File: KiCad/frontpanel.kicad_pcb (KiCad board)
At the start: 2 copper layers, 26 parts, among them P1 CONN_02X13, P2 CONN_02X13

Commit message: some changes and improvments
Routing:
- net (no net): track 0.00 -> 1.27 mm
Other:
- board outline added: 139.7 x 88.9 mm
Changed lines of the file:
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@@
   (general
     (links 87)
-    (no_connects 1)
-    (area 97.689999 26.36 256.92 125.830001)
+    (no_connects 0)
+    (area 97.739999 26.36 256.92 125.780001)
     (thickness 1.6)
-    (drawings 6)
-    (tracks 413)
+    (drawings 18)
+    (tracks 414)
     (zones 0)
     (modules 26)
@@
     (pad_to_mask_clearance 0)
     (aux_axis_origin 0 0)
-    (visible_elements FFFFE77F)
+    (visible_elements FFFFF77F)
     (pcbplotparams
       (layerselection 0x00030_80000001)
@@
       (net 22 "Net-(AFF1-Pad22)"))
   )
-  (gr_line (start 97.79 125.73) (end 97.79 36.83) (angle 90) (layer Eco2.User) (width 0.2))
-  (gr_line (start 237.49 125.73) (end 97.79 125.73) (angle 90) (layer Eco2.User) (width 0.2))
-  (gr_line (start 237.49 36.83) (end 237.49 125.73) (angle 90) (layer Eco2.User) (width 0.2))
-  (gr_line (start 237.49 36.83) (end 97.79 36.83) (angle 90) (layer Eco2.User) (width 0.2))
+  (gr_line (start 99.06 36.83) (end 236.22 36.83) (layer Edge.Cuts) (width 0.1))
+  (gr_line (start 97.79 38.1) (end 97.79 124.46) (layer Edge.Cuts) (width 0.1))
+  (gr_line (start 236.22 125.73) (end 99.06 125.73) (layer Edge.Cuts) (width 0.1))
+  (gr_arc (start 99.06 124.46) (end 99.06 125.73) (angle 90) (layer Edge.Cuts) (width 0.1))
+  (gr_arc (start 236.22 124.46) (end 237.49 124.46) (angle 90) (layer Edge.Cuts) (width 0.1))
+  (gr_line (start 237.49 38.1) (end 237.49 124.46) (layer Edge.Cuts) (width 0.1))
+  (gr_arc (start 236.22 38.1) (end 236.22 36.83) (angle 90) (layer Edge.Cuts) (width 0.1))
+  (gr_arc (start 99.06 38.1) (end 97.79 38.1) (angle 90) (layer Edge.Cuts) (width 0.1))
+  (gr_circle (center 102.87 41.91) (end 101.346 42.164) (layer Edge.Cuts) (width 0.1))
+  (gr_circle (center 102.87 120.65) (end 101.346 120.65) (layer Edge.Cuts) (width 0.1))
+  (gr_circle (center 232.41 120.65) (end 230.886 120.65) (layer Edge.Cuts) (width 0.1))
+  (gr_circle (center 232.41 41.91) (end 230.886 41.91) (layer Edge.Cuts) (width 0.1))
+  (target plus (at 102.87 120.65) (size 5) (width 0.1) (layer Edge.Cuts))
+  (target plus (at 232.41 120.65) (size 5) (width 0.1) (layer Edge.Cuts))
+  (target plus (at 102.87 41.91) (size 5) (width 0.1) (layer Edge.Cuts))
+  (target plus (at 232.41 41.91) (size 5) (width 0.1) (layer Edge.Cuts))
   (dimension 88.9 (width 0.3) (layer Cmts.User)
     (gr_text "88,900 mm" (at 250.27 81.28 270) (layer Cmts.User)
@@
     (arrow2b (pts (xy 237.49 29.21) (xy 236.363496 29.796421)))
   )
+  (segment (start 236.22 124.46) (end 237.49 124.46) (width 0.25) (layer Dwgs.User) (net 0))
   (segment (start 182.88 81.28) (end 194.228601 69.931399) (width 0.25) (layer B.Cu) (net 5))
   (segment (start 194.228601 69.931399) (end 224.708601 69.931399) (width 0.25) (layer B.Cu) (net 5))

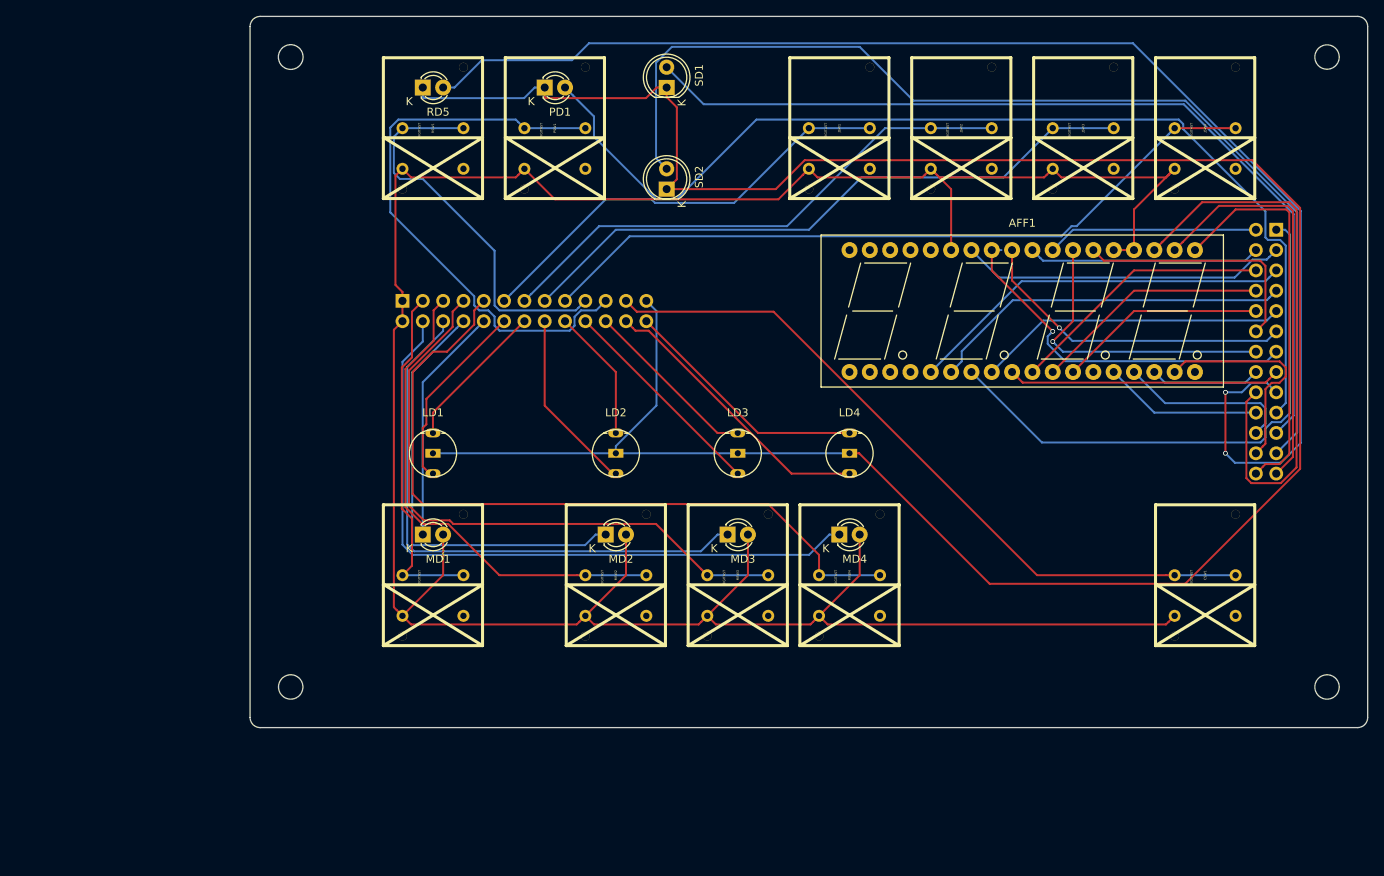
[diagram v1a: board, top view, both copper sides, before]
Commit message: Flipped the pinpads on the frontpanel board ...
... so that we don't have to twist the cables.
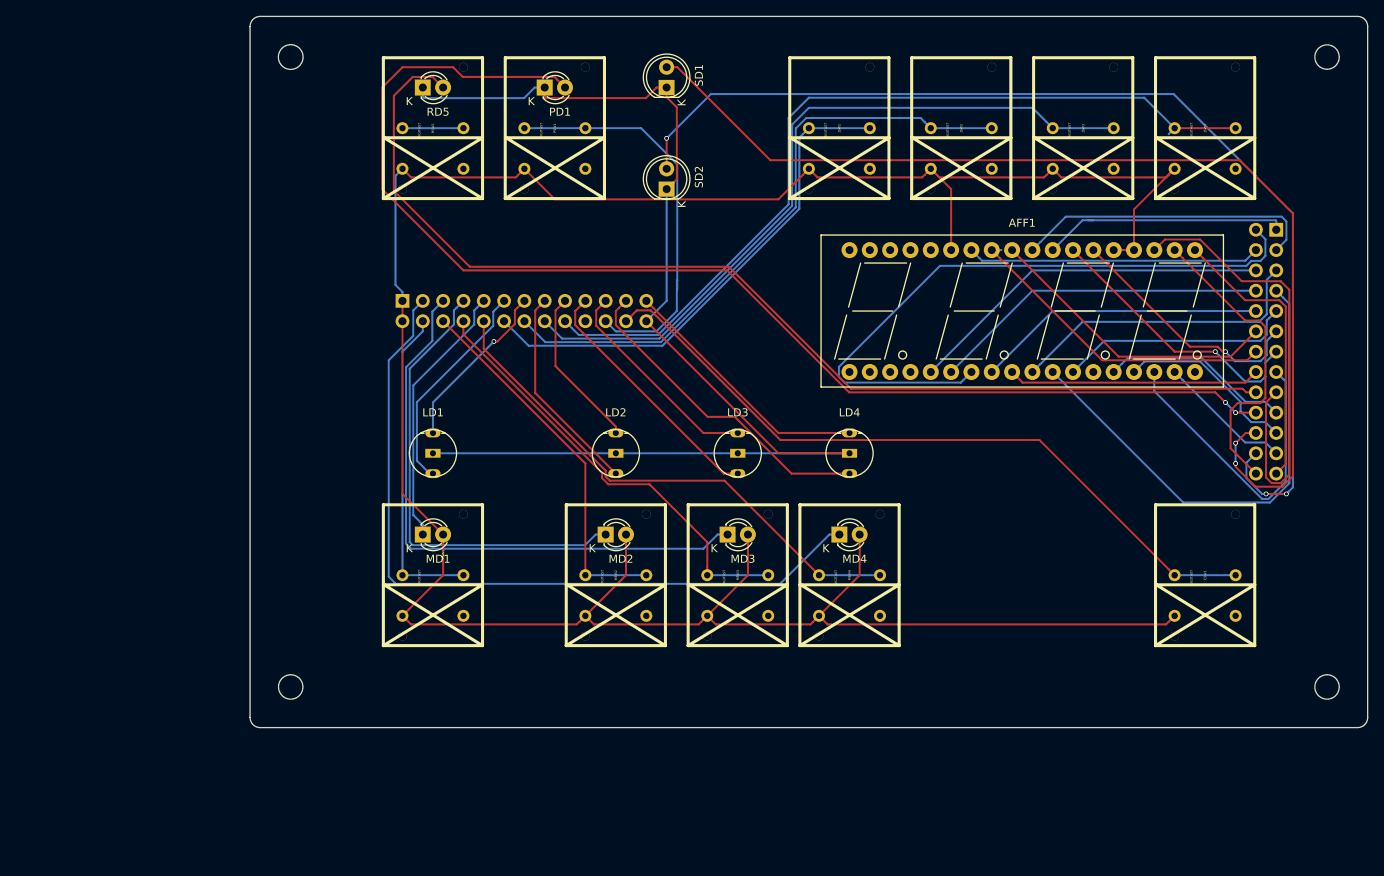
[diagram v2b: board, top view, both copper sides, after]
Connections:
- P1 pad 10: Net-(MD1-Pad1) -> Net-(MSW4-Pad0)
- P1 pad 11: Net-(JSW1-Pad0) -> Net-(LD1-Pad3)
- P1 pad 12: Net-(LD1-Pad3) -> Net-(JSW1-Pad0)
- P1 pad 13: Net-(JSW2-Pad0) -> Net-(LD1-Pad1)
- P1 pad 14: Net-(LD1-Pad1) -> Net-(JSW2-Pad0)
- P1 pad 15: Net-(JSW3-Pad0) -> Net-(LD2-Pad3)
- P1 pad 16: Net-(LD2-Pad3) -> Net-(JSW3-Pad0)
- P1 pad 17: Net-(JSW4-Pad0) -> Net-(LD2-Pad1)
- P1 pad 18: Net-(LD2-Pad1) -> Net-(JSW4-Pad0)
- P1 pad 19: Net-(P1-Pad19) -> Net-(LD3-Pad3)
- P1 pad 20: Net-(LD3-Pad3) -> Net-(P1-Pad20)
- P1 pad 21: Net-(P1-Pad21) -> Net-(LD3-Pad1)
- P1 pad 22: Net-(LD3-Pad1) -> Net-(P1-Pad22)
- P1 pad 23: Net-(CSW1-Pad0) -> Net-(LD4-Pad3)
- P1 pad 24: Net-(LD4-Pad3) -> Net-(CSW1-Pad0)
- P1 pad 25: Net-(LD1-Pad2) -> Net-(LD4-Pad1)
- P1 pad 26: Net-(LD4-Pad1) -> Net-(LD1-Pad2)
- P1 pad 3: Net-(MSW1-Pad0) -> Net-(MD4-Pad1)
- P1 pad 4: Net-(MD4-Pad1) -> Net-(MSW1-Pad0)
- P1 pad 5: Net-(MSW2-Pad0) -> Net-(MD3-Pad1)
- P1 pad 6: Net-(MD3-Pad1) -> Net-(MSW2-Pad0)
- P1 pad 7: Net-(MSW3-Pad0) -> Net-(MD2-Pad1)
- P1 pad 8: Net-(MD2-Pad1) -> Net-(MSW3-Pad0)
- P1 pad 9: Net-(MSW4-Pad0) -> Net-(MD1-Pad1)
- P2 pad 1: Net-(AFF1-Pad7) -> Net-(AFF1-Pad26)
- P2 pad 10: Net-(AFF1-Pad12) -> Net-(AFF1-Pad8)
- P2 pad 11: Net-(AFF1-Pad28) -> Net-(AFF1-Pad24)
- P2 pad 12: Net-(AFF1-Pad24) -> Net-(AFF1-Pad28)
- P2 pad 13: Net-(AFF1-Pad29) -> Net-(AFF1-Pad25)
- P2 pad 14: Net-(AFF1-Pad25) -> Net-(AFF1-Pad29)
- P2 pad 15: Net-(AFF1-Pad9) -> Net-(AFF1-Pad16)
- P2 pad 16: Net-(AFF1-Pad16) -> Net-(AFF1-Pad9)
- P2 pad 17: Net-(P2-Pad17) -> Net-(AFF1-Pad21)
- P2 pad 18: Net-(AFF1-Pad21) -> Net-(P2-Pad18)
- P2 pad 19: Net-(P2-Pad19) -> Net-(AFF1-Pad14)
- P2 pad 2: Net-(AFF1-Pad26) -> Net-(AFF1-Pad7)
- P2 pad 20: Net-(AFF1-Pad14) -> Net-(P2-Pad20)
- P2 pad 21: Net-(P2-Pad21) -> Net-(AFF1-Pad15)
- P2 pad 22: Net-(AFF1-Pad15) -> Net-(P2-Pad22)
- P2 pad 23: Net-(P2-Pad23) -> Net-(AFF1-Pad17)
- P2 pad 24: Net-(AFF1-Pad17) -> Net-(P2-Pad24)
- P2 pad 25: Net-(AFF1-Pad20) -> Net-(AFF1-Pad19)
- P2 pad 26: Net-(AFF1-Pad19) -> Net-(AFF1-Pad20)
- P2 pad 3: Net-(AFF1-Pad30) -> Net-(AFF1-Pad27)
- P2 pad 4: Net-(AFF1-Pad27) -> Net-(AFF1-Pad30)
- P2 pad 5: Net-(AFF1-Pad5) -> Net-(AFF1-Pad10)
- P2 pad 6: Net-(AFF1-Pad10) -> Net-(AFF1-Pad5)
- P2 pad 7: Net-(AFF1-Pad6) -> Net-(AFF1-Pad11)
- P2 pad 8: Net-(AFF1-Pad11) -> Net-(AFF1-Pad6)
- P2 pad 9: Net-(AFF1-Pad8) -> Net-(AFF1-Pad12)
- PD1 pad 2: Net-(P2-Pad19) -> Net-(P2-Pad20)
- PSW1 pad 0: Net-(P1-Pad21) -> Net-(P1-Pad22)
- RD5 pad 2: Net-(P2-Pad17) -> Net-(P2-Pad18)
- RSW1 pad 0: Net-(P1-Pad19) -> Net-(RSW1-Pad0)
- SD1 pad 2: Net-(P2-Pad21) -> Net-(P2-Pad22)
- SD2 pad 2: Net-(P2-Pad23) -> Net-(P2-Pad24)
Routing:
- net Net-(P2-Pad17): track 173.1 -> 0.00 mm, vias 2 -> 0
- net Net-(P2-Pad20): track 0.00 -> 158.5 mm, vias 0 -> 2
- net Net-(LD1-Pad2): track 307.9 -> 151.2 mm
- net Net-(P2-Pad18): track 0.00 -> 137.8 mm
- net Net-(P2-Pad24): track 0.00 -> 135.4 mm, vias 0 -> 3
- net Net-(P2-Pad23): track 134.5 -> 0.00 mm
- net Net-(P2-Pad22): track 0.00 -> 133.5 mm, vias 0 -> 2
- net Net-(P2-Pad19): track 131.7 -> 0.00 mm
- net Net-(P2-Pad21): track 114.2 -> 0.00 mm
- net Net-(P1-Pad21): track 72.4 -> 0.00 mm
- net Net-(P1-Pad22): track 0.00 -> 51.0 mm
- net Net-(P1-Pad19): track 49.2 -> 0.00 mm
- net Net-(AFF1-Pad11): track 29.6 -> 62.1 mm
- net Net-(MSW4-Pad0): track 93.0 -> 65.1 mm
- net Net-(AFF1-Pad16): track 13.8 -> 39.5 mm
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
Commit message: Reinforced power wires on frontpanel board
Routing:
- net Net-(AFF1-Pad22): track 327.0 -> 334.1 mm
- net Net-(LD1-Pad2): track 151.2 -> 150.4 mm
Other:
- net class Power added: clearance 0.2, trace_width 0.58, via_dia 0.6, via_drill 0.4

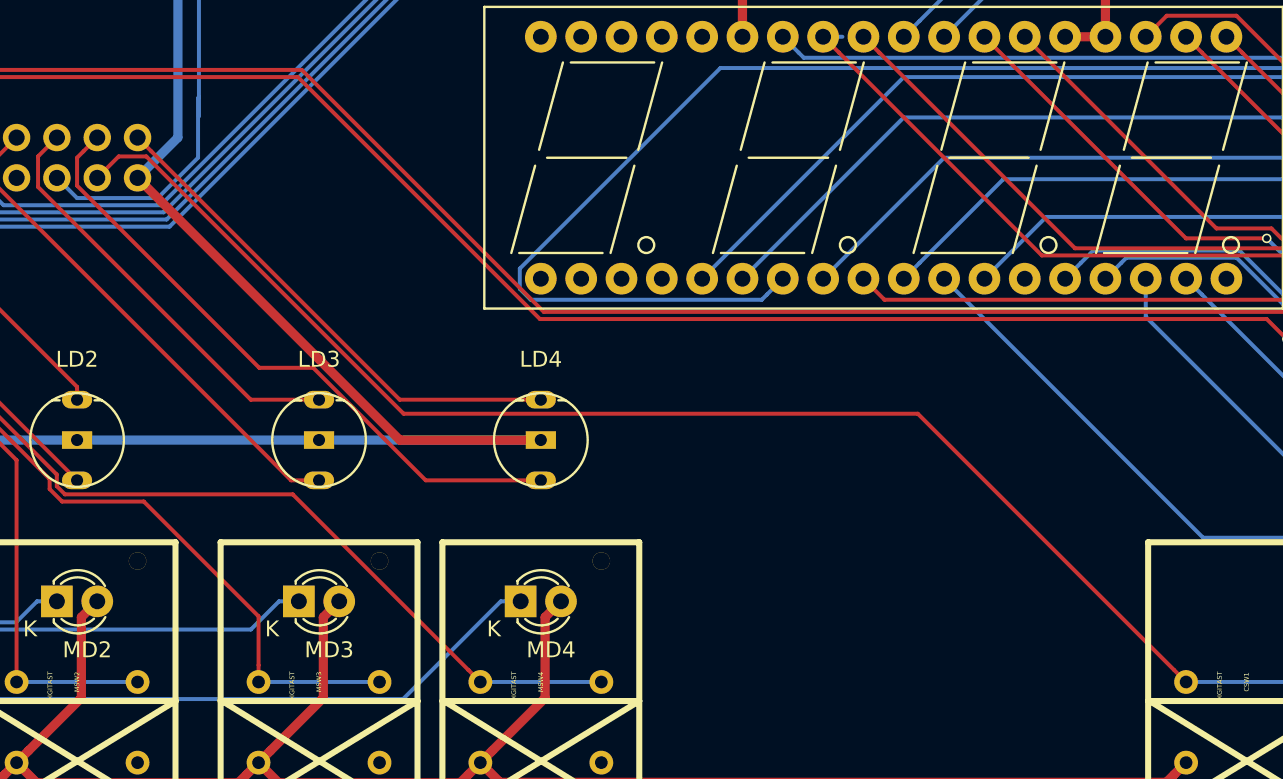
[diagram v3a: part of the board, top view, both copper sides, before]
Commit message: stripped some wires
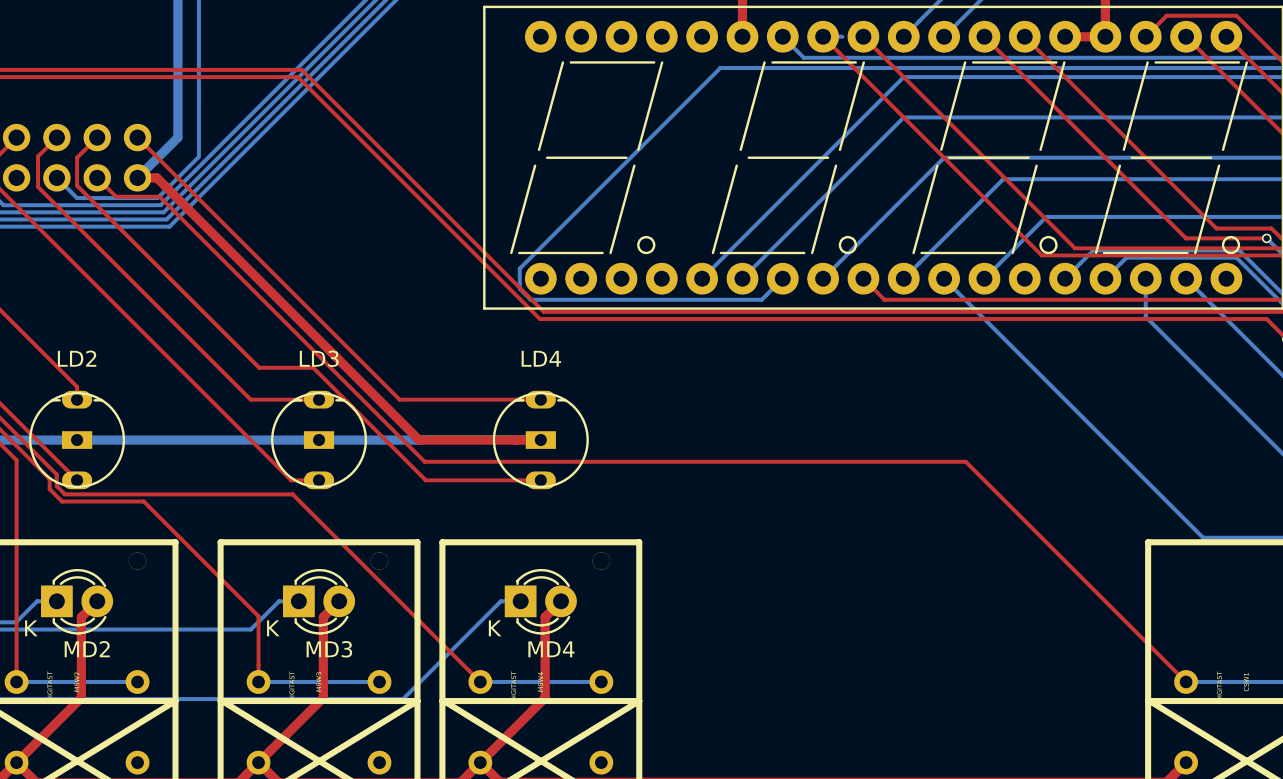
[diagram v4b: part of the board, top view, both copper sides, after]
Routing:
- net Net-(P1-Pad22): track 51.0 -> 49.7 mm
- net Net-(CSW1-Pad0): track 90.5 -> 89.4 mm
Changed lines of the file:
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@@
   (general
     (links 86)
-    (no_connects 5)
-    (area 97.739999 26.36 256.92 125.780001)
+    (no_connects 0)
+    (area 97.739999 36.779999 237.540001 125.780001)
     (thickness 1.6)
     (drawings 18)
-    (tracks 433)
+    (tracks 432)
     (zones 0)
     (modules 26)
@@
   (segment (start 189.285001 67.365001) (end 188.959999 67.039999) (width 0.25) (layer B.Cu) (net 29))
   (segment (start 188.959999 67.039999) (end 187.96 66.04) (width 0.25) (layer B.Cu) (net 29))
-  (segment (start 144.78 74.93) (end 146.131399 73.578601) (width 0.25) (layer F.Cu) (net 35))
-  (segment (start 146.131399 73.578601) (end 147.872191 73.578601) (width 0.25) (layer F.Cu) (net 35))
-  (segment (start 196.46381 89.78381) (end 212.609431 105.929431) (width 0.25) (layer F.Cu) (net 35))
-  (segment (start 147.872191 73.578601) (end 164.0774 89.78381) (width 0.25) (layer F.Cu) (net 35))
-  (segment (start 164.0774 89.78381) (end 196.46381 89.78381) (width 0.25) (layer F.Cu) (net 35))
-  (segment (start 212.609431 105.929431) (end 213.36 106.68) (width 0.25) (layer F.Cu) (net 35))
+  (segment (start 165.4048 92.8116) (end 199.4916 92.8116) (width 0.25) (layer F.Cu) (net 35))
+  (segment (start 199.4916 92.8116) (end 213.36 106.68) (width 0.25) (layer F.Cu) (net 35))
+  (segment (start 148.711801 76.118601) (end 165.4048 92.8116) (width 0.25) (layer F.Cu) (net 35))
+  (segment (start 145.968601 76.118601) (end 148.711801 76.118601) (width 0.25) (layer F.Cu) (net 35))
+  (segment (start 144.78 74.93) (end 145.968601 76.118601) (width 0.25) (layer F.Cu) (net 35))
   (segment (start 213.36 106.68) (end 220.98 106.68) (width 0.25) (layer B.Cu) (net 35))
   (segment (start 166.889431 51.550569) (end 167.64 50.8) (width 0.25) (layer B.Cu) (net 37))
@@
   (segment (start 120.65 85.09) (end 128.27 77.47) (width 0.25) (layer B.Cu) (net 45))
   (via (at 128.27 77.47) (size 0.6) (drill 0.4) (layers F.Cu B.Cu) (net 45))
+  (segment (start 171.1875 91.44) (end 172.72 91.44) (width 0.58) (layer F.Cu) (net 46))
+  (segment (start 165.051314 91.44) (end 171.1875 91.44) (width 0.58) (layer F.Cu) (net 46))
+  (segment (start 148.541314 74.93) (end 165.051314 91.44) (width 0.58) (layer F.Cu) (net 46))
+  (segment (start 147.32 74.93) (end 148.541314 74.93) (width 0.58) (layer F.Cu) (net 46))
   (segment (start 119.38 45.72) (end 120.870001 47.210001) (width 0.58) (layer F.Cu) (net 46))
   (segment (start 120.870001 47.210001) (end 136.110001 47.210001) (width 0.58) (layer F.Cu) (net 46))
@@
   (segment (start 143.51 91.44) (end 158.75 91.44) (width 0.58) (layer B.Cu) (net 46))
   (segment (start 172.72 91.44) (end 158.75 91.44) (width 0.58) (layer B.Cu) (net 46))
-  (segment (start 147.32 74.93) (end 163.83 91.44) (width 0.58) (layer F.Cu) (net 46))
-  (segment (start 163.83 91.44) (end 172.72 91.44) (width 0.58) (layer F.Cu) (net 46))
   (segment (start 149.81 58.42) (end 149.86 58.42) (width 0.25) (layer B.Cu) (net 46))
   (segment (start 134.62 45.72) (end 134.62 46.97) (width 0.25) (layer B.Cu) (net 46))
@@
   (segment (start 142.23249 94.346086) (end 142.750214 94.86381) (width 0.25) (layer F.Cu) (net 64))
   (segment (start 168.91 106.68) (end 176.53 106.68) (width 0.25) (layer B.Cu) (net 64))
+  (segment (start 151.185001 69.85) (end 151.185001 73.604999) (width 0.25) (layer B.Cu) (net 69))
   (segment (start 151.185001 55.317999) (end 151.185001 69.85) (width 0.25) (layer B.Cu) (net 69))
-  (segment (start 151.185001 69.85) (end 151.185001 71.064999) (width 0.25) (layer B.Cu) (net 69))
-  (segment (start 151.13 73.66) (end 151.13 69.905001) (width 0.25) (layer B.Cu) (net 69))
-  (segment (start 151.13 69.905001) (end 151.185001 69.85) (width 0.25) (layer B.Cu) (net 69))
   (segment (start 148.59 76.2) (end 151.13 73.66) (width 0.25) (layer B.Cu) (net 69))
   (segment (start 143.51 76.2) (end 148.59 76.2) (width 0.25) (layer B.Cu) (net 69))
